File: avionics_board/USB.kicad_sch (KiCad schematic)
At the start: 3 parts, among them J13 10155435-00011LF

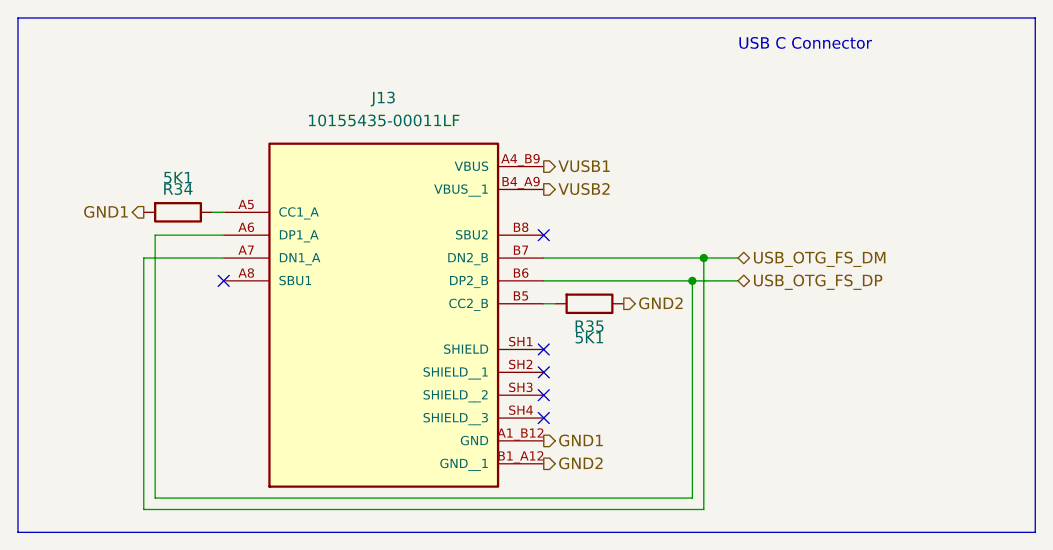
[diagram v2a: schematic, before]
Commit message: tweaking SCI and AUX for production, using common sheets as much as possible
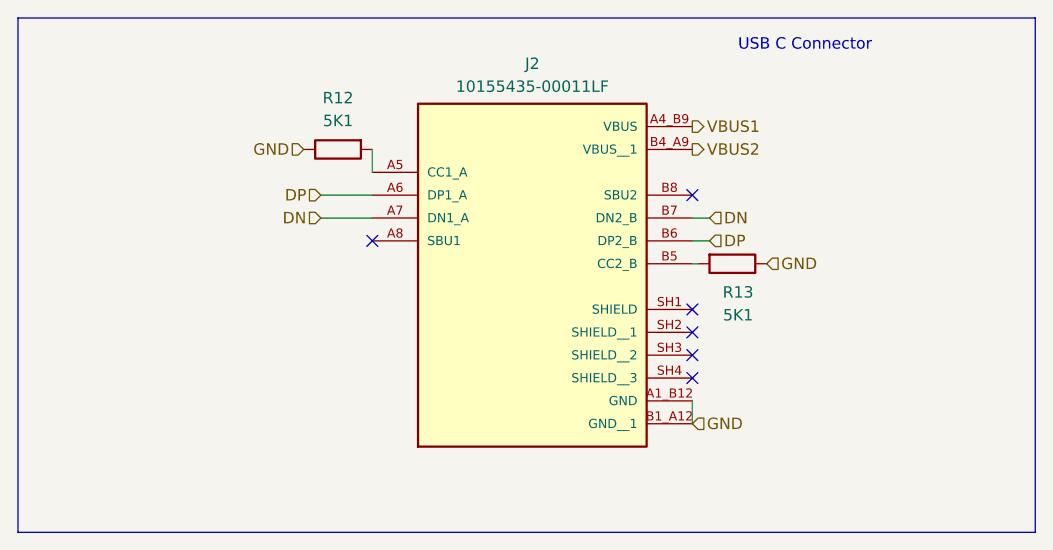
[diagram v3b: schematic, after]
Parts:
- removed J13: 10155435-00011LF, Common:AMPHENOL_10155435-00011LF, symbol Common:10155435-00011LF
- removed R34, R35: 5K1, Resistor_SMD:R_0402_1005Metric_Pad0.72x0.64mm_HandSolder, symbol Device:R
- added J2: 10155435-00011LF, Project:AMPHENOL_10155435-00011LF, symbol Project:10155435-00011LF
- added R12, R13: 5K1, Resistor_SMD:R_0603_1608Metric_Pad0.98x0.95mm_HandSolder, symbol Device:R
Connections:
- new net: J2.B5 (CC2_B), R13.2
- new net: J2.A5 (CC1_A), R12.2
- new net DN: J2.A7 (DN1_A), J2.B7 (DN2_B)
- new net DP: J2.A6 (DP1_A), J2.B6 (DP2_B)
- new net GND: J2.A1_B12 (GND), J2.B1_A12 (GND__1), R12.1, R13.1
- new net VBUS1: J2.A4_B9 (VBUS)
- new net VBUS2: J2.B4_A9 (VBUS__1)

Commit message: clenup BOM for SCI and AUX
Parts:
- R12, R13: footprint Resistor_SMD:R_0603_1608Metric_Pad0.98x0.95mm_HandSolder -> Resistor_SMD:R_0402_1005Metric_Pad0.72x0.64mm_HandSolder; Part Number RC0603FR-075K1L -> RC0402FR-075K1L
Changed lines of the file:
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@@
 			)
 		)
-		(property "Footprint" "Resistor_SMD:R_0603_1608Metric_Pad0.98x0.95mm_HandSolder"
+		(property "Footprint" "Resistor_SMD:R_0402_1005Metric_Pad0.72x0.64mm_HandSolder"
 			(at 175.895 92.837 90)
 			(effects
@@
 			)
 		)
-		(property "Part Number" "RC0603FR-075K1L"
+		(property "Part Number" "RC0402FR-075K1L"
 			(at 175.895 94.615 0)
 			(effects
@@
 		)
 		(property "Tolerance" "1"
-			(at 175.895 94.615 0)
-			(effects
-				(font
-					(size 1.27 1.27)
-				)
-				(hide yes)
-			)
-		)
-		(property "MANUFACTURER" ""
-			(at 175.895 94.615 0)
-			(effects
-				(font
-					(size 1.27 1.27)
-				)
-				(hide yes)
-			)
-		)
-		(property "MAXIMUM_PACKAGE_HEIGHT" ""
-			(at 175.895 94.615 0)
-			(effects
-				(font
-					(size 1.27 1.27)
-				)
-				(hide yes)
-			)
-		)
-		(property "Manufactorer" ""
-			(at 175.895 94.615 0)
-			(effects
-				(font
-					(size 1.27 1.27)
-				)
-				(hide yes)
-			)
-		)
-		(property "PARTREV" ""
-			(at 175.895 94.615 0)
-			(effects
-				(font
-					(size 1.27 1.27)
-				)
-				(hide yes)
-			)
-		)
-		(property "STANDARD" ""
 			(at 175.895 94.615 0)
 			(effects
@@
 			)
 		)
-		(property "Footprint" "Resistor_SMD:R_0603_1608Metric_Pad0.98x0.95mm_HandSolder"
+		(property "Footprint" "Resistor_SMD:R_0402_1005Metric_Pad0.72x0.64mm_HandSolder"
 			(at 132.08 80.137 90)
 			(effects
@@
 			)
 		)
-		(property "Part Number" "RC0603FR-075K1L"
+		(property "Part Number" "RC0402FR-075K1L"
 			(at 132.08 81.915 0)
 			(effects
@@
 		)
 		(property "Tolerance" "1"
-			(at 132.08 81.915 0)
-			(effects
-				(font
-					(size 1.27 1.27)
-				)
-				(hide yes)
-			)
-		)
-		(property "MANUFACTURER" ""
-			(at 132.08 81.915 0)
-			(effects
-				(font
-					(size 1.27 1.27)
-				)
-				(hide yes)
-			)
-		)
-		(property "MAXIMUM_PACKAGE_HEIGHT" ""
-			(at 132.08 81.915 0)
-			(effects
-				(font
-					(size 1.27 1.27)
-				)
-				(hide yes)
-			)
-		)
-		(property "Manufactorer" ""
-			(at 132.08 81.915 0)
-			(effects
-				(font
-					(size 1.27 1.27)
-				)
-				(hide yes)
-			)
-		)
-		(property "PARTREV" ""
-			(at 132.08 81.915 0)
-			(effects
-				(font
-					(size 1.27 1.27)
-				)
-				(hide yes)
-			)
-		)
-		(property "STANDARD" ""
 			(at 132.08 81.915 0)
 			(effects
@@
 			(at 153.67 89.535 0)
 			(effects
-				(font
-					(size 1.27 1.27)
-				)
-				(hide yes)
-			)
-		)
-		(property "MANUFACTURER" ""
-			(at 153.67 89.535 0)
-			(effects
-				(font
-					(size 1.27 1.27)
-				)
-				(hide yes)
-			)
-		)
-		(property "MAXIMUM_PACKAGE_HEIGHT" ""
-			(at 153.67 89.535 0)
-			(effects
-				(font
-					(size 1.27 1.27)
-				)
-				(hide yes)
-			)
-		)
-		(property "Manufactorer" ""
-			(at 153.67 89.535 0)
-			(effects
-				(font
-					(size 1.27 1.27)
-				)
-				(hide yes)
-			)
-		)
-		(property "PARTREV" ""
-			(at 153.67 89.535 0)
-			(effects
-				(font
-					(size 1.27 1.27)
-				)
-				(hide yes)
-			)
-		)
-		(property "STANDARD" ""
-			(at 153.67 89.535 0)
-			(effects

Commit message: QC, add second 3V regulator to AUX, INT pullups on AUX SCI AVI
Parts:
- renumbered R12 to R15, R13 to R16
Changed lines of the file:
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@@
 		(on_board yes)
 		(dnp no)
-		(property "Reference" "R13"
+		(property "Reference" "R16"
 			(at 176.53 97.79 90)
 			(effects
@@
 			(project "sci_board"
 				(path "/b4b2c88d-f6cd-4e60-862d-e21f68728580/840799ac-4fe6-4a8e-96a2-299affeec8e4/6b5440ce-79ea-4c41-89e9-7a3077535944"
-					(reference "R13")
+					(reference "R16")
+					(unit 1)
+				)
+			)
+			(project "AVIONICS_BOARD"
+				(path "/f6cc00ab-17f1-4973-862f-7ac95fe70668/00000000-0000-0000-0000-00005ea31c93/8a47ccc3-f8e0-403c-b9fa-fe30da676570"
+					(reference "R41")
 					(unit 1)
 				)
@@
 		(on_board yes)
 		(dnp no)
-		(property "Reference" "R12"
+		(property "Reference" "R15"
 			(at 132.08 76.2 90)
 			(effects
@@
 			(project "sci_board"
 				(path "/b4b2c88d-f6cd-4e60-862d-e21f68728580/840799ac-4fe6-4a8e-96a2-299affeec8e4/6b5440ce-79ea-4c41-89e9-7a3077535944"
-					(reference "R12")
+					(reference "R15")
+					(unit 1)
+				)
+			)
+			(project "AVIONICS_BOARD"
+				(path "/f6cc00ab-17f1-4973-862f-7ac95fe70668/00000000-0000-0000-0000-00005ea31c93/8a47ccc3-f8e0-403c-b9fa-fe30da676570"
+					(reference "R40")
 					(unit 1)
 				)
@@
 					(unit 1)
 				)
+			)
+			(project "AVIONICS_BOARD"
+				(path "/f6cc00ab-17f1-4973-862f-7ac95fe70668/00000000-0000-0000-0000-00005ea31c93/8a47ccc3-f8e0-403c-b9fa-fe30da676570"
+					(reference "J9")
+					(unit 1)
+				)

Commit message: propate the changes to RF
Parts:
- J11: renamed from J2; footprint Project:AMPHENOL_10155435-00011LF -> Common:AMPHENOL_10155435-00011LF; symbol Project:10155435-00011LF -> Common:10155435-00011LF
- renumbered R15 to R29, R16 to R30
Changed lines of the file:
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@@
 		(on_board yes)
 		(dnp no)
-		(property "Reference" "R16"
+		(property "Reference" "R30"
 			(at 176.53 97.79 90)
 			(effects
@@
 		)
 		(instances
+			(project "openlst-hw"
+				(path "/a863a5ec-a5d4-4f54-be53-e8c01d5e3ac4/53f12969-e593-459a-9671-cc23a5a9aea0/f4ff56ce-2fa2-4b99-a709-c113709260c1/628ad651-1312-4f46-81d9-5410d3446e8f"
+					(reference "R30")
+					(unit 1)
+				)
+			)
 			(project "sci_board"
 				(path "/b4b2c88d-f6cd-4e60-862d-e21f68728580/840799ac-4fe6-4a8e-96a2-299affeec8e4/6b5440ce-79ea-4c41-89e9-7a3077535944"
@@
 		(on_board yes)
 		(dnp no)
-		(property "Reference" "R15"
+		(property "Reference" "R29"
 			(at 132.08 76.2 90)
 			(effects
@@
 		)
 		(instances
+			(project "openlst-hw"
+				(path "/a863a5ec-a5d4-4f54-be53-e8c01d5e3ac4/53f12969-e593-459a-9671-cc23a5a9aea0/f4ff56ce-2fa2-4b99-a709-c113709260c1/628ad651-1312-4f46-81d9-5410d3446e8f"
+					(reference "R29")
+					(unit 1)
+				)
+			)
 			(project "sci_board"
 				(path "/b4b2c88d-f6cd-4e60-862d-e21f68728580/840799ac-4fe6-4a8e-96a2-299affeec8e4/6b5440ce-79ea-4c41-89e9-7a3077535944"
@@
 	)
 	(symbol
-		(lib_id "Project:10155435-00011LF")
+		(lib_id "Common:10155435-00011LF")
 		(at 153.67 89.535 0)
 		(unit 1)
@@
 		(dnp no)
 		(fields_autoplaced yes)
-		(property "Reference" "J2"
+		(property "Reference" "J11"
 			(at 153.67 72.39 0)
 			(effects
@@
 			)
 		)
-		(property "Footprint" "Project:AMPHENOL_10155435-00011LF"
+		(property "Footprint" "Common:AMPHENOL_10155435-00011LF"
 			(at 153.67 89.535 0)
 			(effects
@@
 		)
 		(instances
+			(project "openlst-hw"
+				(path "/a863a5ec-a5d4-4f54-be53-e8c01d5e3ac4/53f12969-e593-459a-9671-cc23a5a9aea0/f4ff56ce-2fa2-4b99-a709-c113709260c1/628ad651-1312-4f46-81d9-5410d3446e8f"
+					(reference "J11")
+					(unit 1)
+				)
+			)
 			(project "sci_board"
 				(path "/b4b2c88d-f6cd-4e60-862d-e21f68728580/840799ac-4fe6-4a8e-96a2-299affeec8e4/6b5440ce-79ea-4c41-89e9-7a3077535944"

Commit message: local switches and monitors for SCI and RF
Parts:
- renumbered R29 to R43, R30 to R44
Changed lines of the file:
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@@
 		(on_board yes)
 		(dnp no)
-		(property "Reference" "R30"
+		(property "Reference" "R44"
 			(at 176.53 97.79 90)
 			(effects
@@
 			(project "openlst-hw"
 				(path "/a863a5ec-a5d4-4f54-be53-e8c01d5e3ac4/53f12969-e593-459a-9671-cc23a5a9aea0/f4ff56ce-2fa2-4b99-a709-c113709260c1/628ad651-1312-4f46-81d9-5410d3446e8f"
-					(reference "R30")
+					(reference "R44")
 					(unit 1)
 				)
@@
 			(project "sci_board"
 				(path "/b4b2c88d-f6cd-4e60-862d-e21f68728580/840799ac-4fe6-4a8e-96a2-299affeec8e4/6b5440ce-79ea-4c41-89e9-7a3077535944"
-					(reference "R16")
+					(reference "R19")
 					(unit 1)
 				)
@@
 		(on_board yes)
 		(dnp no)
-		(property "Reference" "R29"
+		(property "Reference" "R43"
 			(at 132.08 76.2 90)
 			(effects
@@
 			(project "openlst-hw"
 				(path "/a863a5ec-a5d4-4f54-be53-e8c01d5e3ac4/53f12969-e593-459a-9671-cc23a5a9aea0/f4ff56ce-2fa2-4b99-a709-c113709260c1/628ad651-1312-4f46-81d9-5410d3446e8f"
-					(reference "R29")
+					(reference "R43")
 					(unit 1)
 				)
@@
 			(project "sci_board"
 				(path "/b4b2c88d-f6cd-4e60-862d-e21f68728580/840799ac-4fe6-4a8e-96a2-299affeec8e4/6b5440ce-79ea-4c41-89e9-7a3077535944"
-					(reference "R15")
-					(unit 1)
-				)
+					(reference "R18")
+					(unit 1)
+				)
